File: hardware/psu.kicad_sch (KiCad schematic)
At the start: 13 parts, among them U701 XC6206

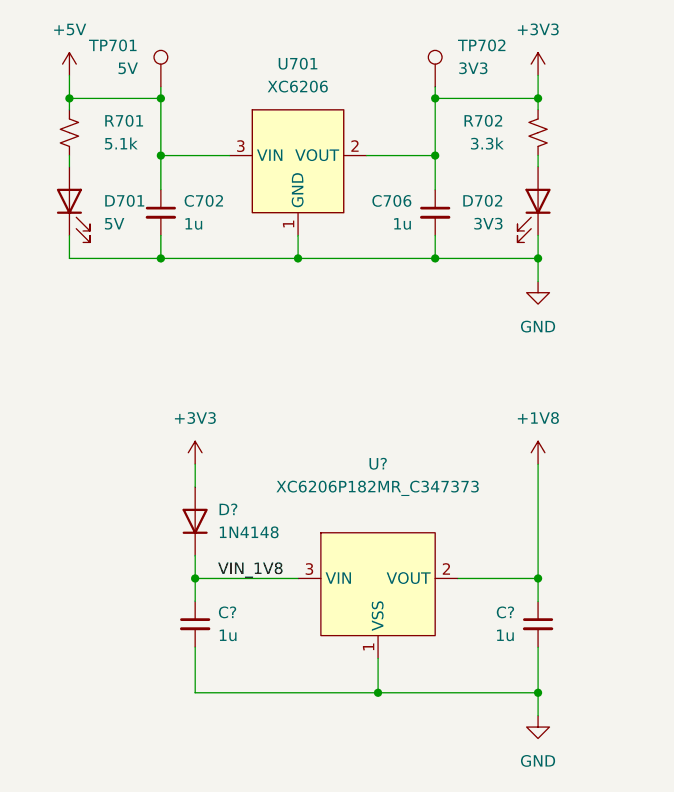
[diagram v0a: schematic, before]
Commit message: new hardware layout for IIS2ICLX
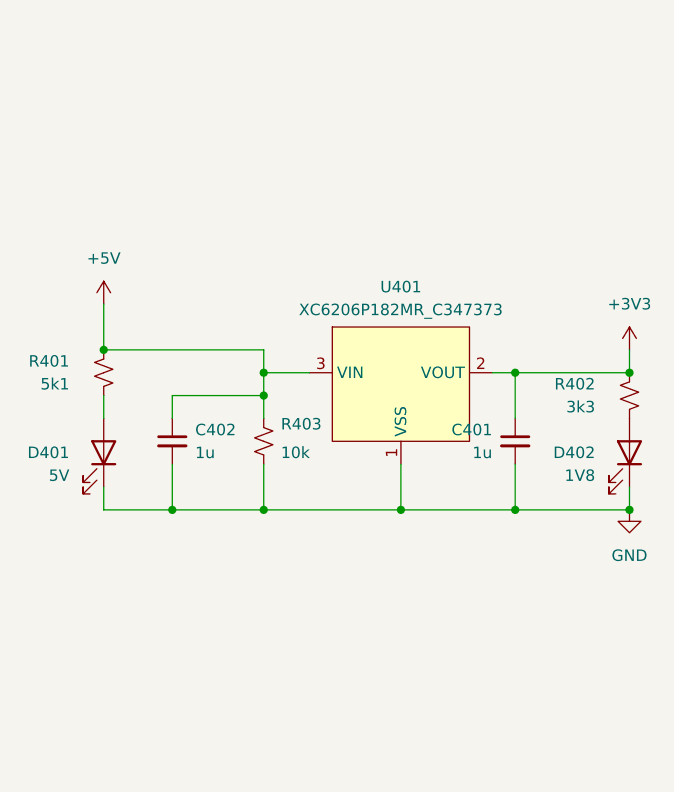
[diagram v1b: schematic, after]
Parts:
- removed C? (x2): 1u, Capacitor_SMD:C_0402_1005Metric, symbol Device:C_Small
- removed D?: 1N4148, symbol Device:D
- removed TP701: 5V, TestPoint:TestPoint_Pad_D1.0mm, symbol Connector:TestPoint
- removed TP702: 3V3, TestPoint:TestPoint_Pad_D1.0mm, symbol Connector:TestPoint
- removed U701: XC6206, Package_TO_SOT_SMD:SOT-23, symbol matei:XC6206
- removed U?: XC6206P182MR_C347373, easyeda2kicad:SOT-23-3_L3.0-W1.7-P0.95-LS2.9-BR, symbol easyeda2kicad:XC6206P182MR_C347373
- added R403: 10k, Resistor_SMD:R_0402_1005Metric, symbol Device:R_Small_US
- added U401: XC6206P182MR_C347373, easyeda2kicad:SOT-23-3_L3.0-W1.7-P0.95-LS2.9-BR, symbol easyeda2kicad:XC6206P182MR_C347373
- C401: renamed from C706; LCSC ID (none) -> C52923
- C402: renamed from C702; LCSC ID (none) -> C52923
- D401: renamed from D701; LCSC ID (none) -> C2290
- D402: renamed from D702; value 3V3 -> 1V8; LCSC ID (none) -> C2290
- R401: renamed from R701; value 5.1k -> 5k1; LCSC ID (none) -> C25905
- R402: renamed from R702; value 3.3k -> 3k3; LCSC ID (none) -> C25890
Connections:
- net +3V3: now also U401.2 (VOUT)
- net +5V: now also R403.1, U401.3 (VIN)
- net GND: now also R403.2, U401.1 (VSS)
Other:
- moved on the sheet: C401, C402, D401, D402, R401, R402
